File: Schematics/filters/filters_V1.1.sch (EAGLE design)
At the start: 110 parts, among them IC1 NE5532N, IC2 NE5532N, IC3 NE5532N, IC4 NE5532N, IC5 NE5532N, IC6 NE5532N, IC7 NE5532N, J1 3_PIN_AMPCONN, J2 4_PIN_AMPCONN, J3 3_PIN_AMPCONN

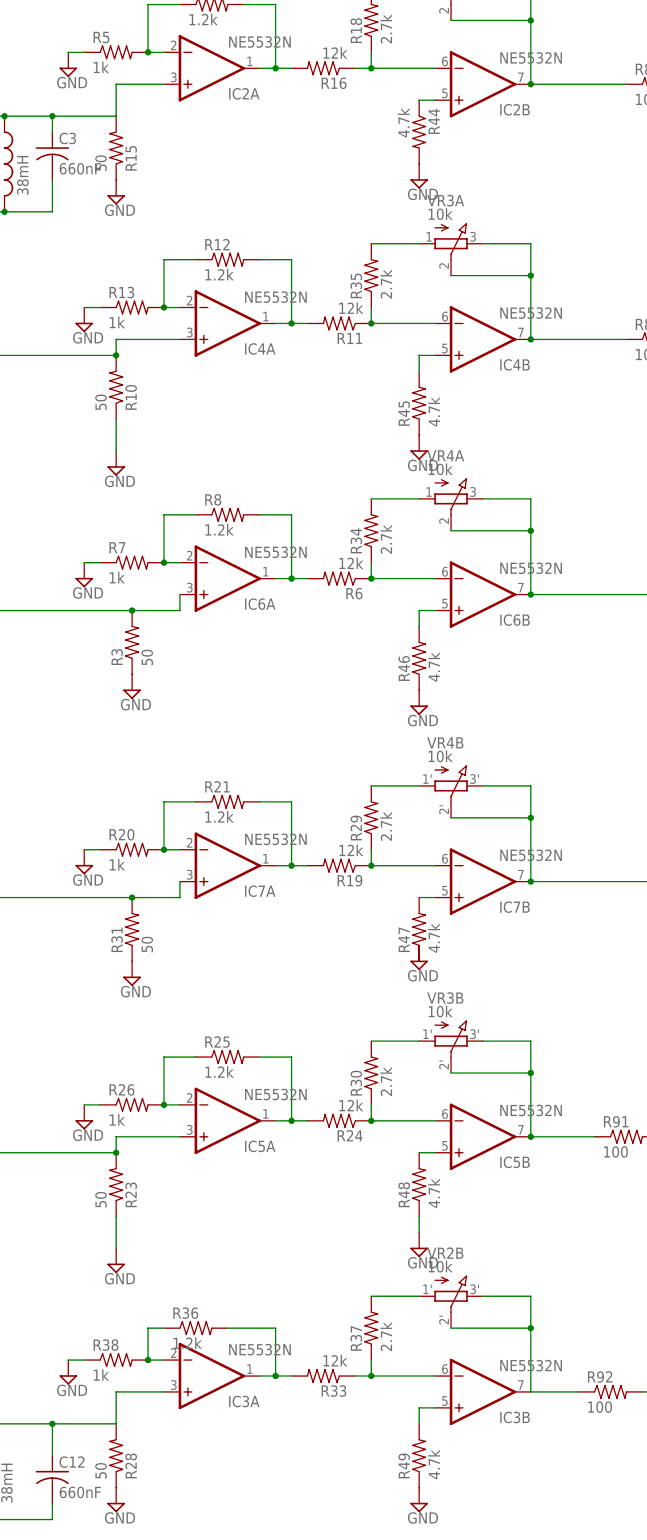
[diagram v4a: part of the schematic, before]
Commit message: Updated low pass filter amplifier with increased gain. Added filter response measurements
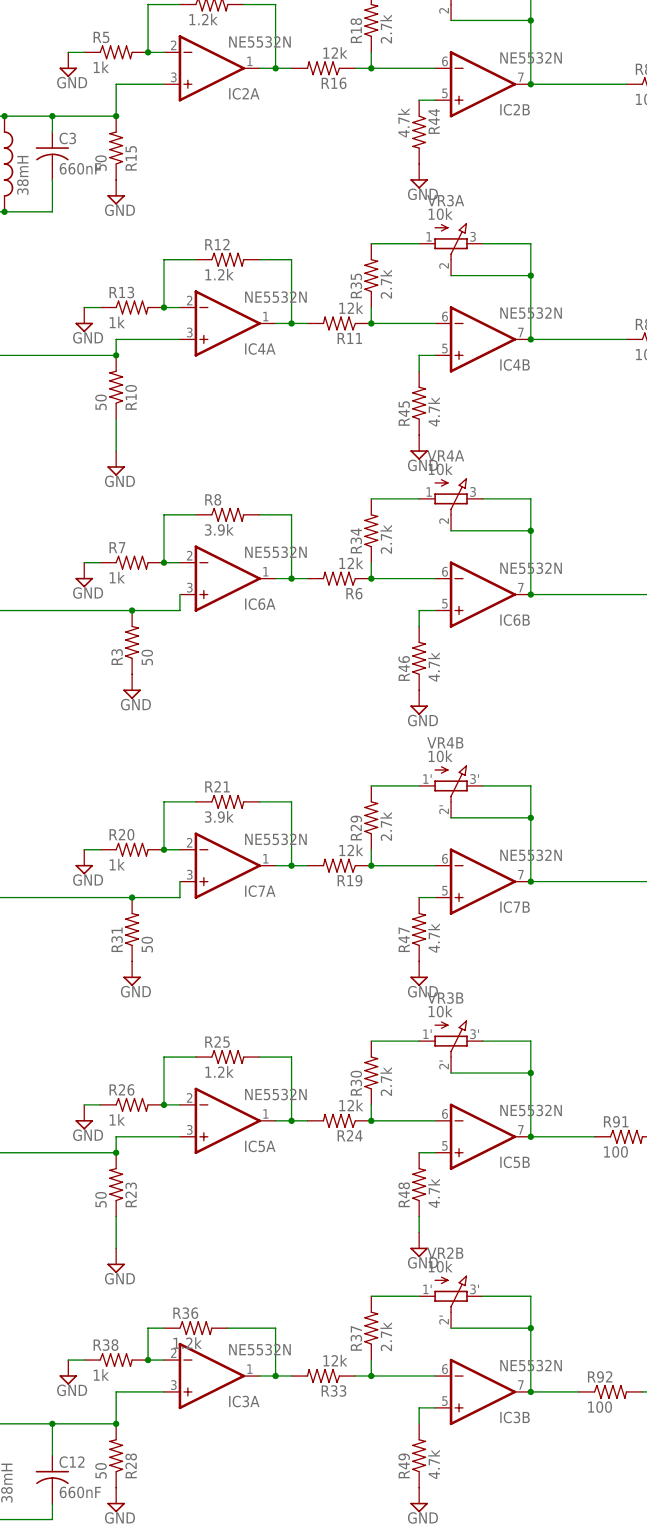
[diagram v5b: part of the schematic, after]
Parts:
- R21, R8: value 1.2k -> 3.9k
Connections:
- net GND: now also R47.1
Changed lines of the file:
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@@
 <part name="R6" library="rcl" deviceset="R-US_" device="0204/2V" value="12k"/>
 <part name="R7" library="rcl" deviceset="R-US_" device="0204/2V" value="1k"/>
-<part name="R8" library="rcl" deviceset="R-US_" device="0204/2V" value="1.2k"/>
+<part name="R8" library="rcl" deviceset="R-US_" device="0204/2V" value="3.9k"/>
 <part name="R9" library="rcl" deviceset="R-US_" device="0204/2V" value="50"/>
 <part name="R10" library="rcl" deviceset="R-US_" device="0204/2V" value="50"/>
@@
 <part name="R19" library="rcl" deviceset="R-US_" device="0204/2V" value="12k"/>
 <part name="R20" library="rcl" deviceset="R-US_" device="0204/2V" value="1k"/>
-<part name="R21" library="rcl" deviceset="R-US_" device="0204/2V" value="1.2k"/>
+<part name="R21" library="rcl" deviceset="R-US_" device="0204/2V" value="3.9k"/>
 <part name="R22" library="rcl" deviceset="R-US_" device="0204/2V" value="50"/>
 <part name="R23" library="rcl" deviceset="R-US_" device="0204/2V" value="50"/>
@@
 <part name="R37" library="rcl" deviceset="R-US_" device="0204/2V" value="2.7k"/>
 <part name="R38" library="rcl" deviceset="R-US_" device="0204/2V" value="1k"/>
-<part name="GND4" library="supply2" deviceset="GND" device=""/>
 <part name="GND5" library="supply2" deviceset="GND" device=""/>
 <part name="GND6" library="supply2" deviceset="GND" device=""/>
@@
 <part name="R45" library="rcl" deviceset="R-US_" device="0204/2V" value="4.7k"/>
 <part name="R46" library="rcl" deviceset="R-US_" device="0204/2V" value="4.7k"/>
-<part name="R47" library="rcl" deviceset="R-US_" device="0204/2V" value="4.7k"/>
 <part name="R48" library="rcl" deviceset="R-US_" device="0204/2V" value="4.7k"/>
 <part name="R49" library="rcl" deviceset="R-US_" device="0204/2V" value="4.7k"/>
@@
 <part name="J2" library="Amplifier_Parts" deviceset="4_PIN_AMPCONN" device=""/>
 <part name="GND27" library="supply2" deviceset="GND" device=""/>
+<part name="R47" library="rcl" deviceset="R-US_" device="0204/2V" value="4.7k"/>
+<part name="GND4" library="supply2" deviceset="GND" device=""/>
 </parts>
 <sheets>
@@
 <instance part="R37" gate="G$1" x="304.8" y="88.9" rot="R90"/>
 <instance part="R38" gate="G$1" x="264.16" y="83.82"/>
-<instance part="GND4" gate="GND" x="312.42" y="147.32"/>
 <instance part="GND5" gate="GND" x="312.42" y="101.6"/>
 <instance part="GND6" gate="GND" x="312.42" y="60.96"/>
@@
 <instance part="R45" gate="G$1" x="312.42" y="236.22" rot="R90"/>
 <instance part="R46" gate="G$1" x="312.42" y="195.58" rot="R90"/>
-<instance part="R47" gate="G$1" x="312.42" y="152.4" rot="R90"/>
 <instance part="R48" gate="G$1" x="312.42" y="111.76" rot="R90"/>
 <instance part="R49" gate="G$1" x="312.42" y="68.58" rot="R90"/>
@@
 <instance part="J2" gate="G$1" x="482.6" y="180.34" rot="MR0"/>
 <instance part="GND27" gate="GND" x="474.98" y="170.18"/>
+<instance part="R47" gate="G$1" x="312.42" y="152.4" rot="R90"/>
+<instance part="GND4" gate="GND" x="312.42" y="144.78"/>
 </instances>
 <busses>
@@
 <pinref part="J2" gate="G$1" pin="4"/>
 <wire x1="474.98" y1="175.26" x2="477.52" y2="175.26" width="0.1524" layer="91"/>
+</segment>
+<segment>
+<pinref part="R47" gate="G$1" pin="1"/>
+<pinref part="GND4" gate="GND" pin="GND"/>
 </segment>
 </net>
@@
 <pinref part="IC2" gate="A" pin="+IN"/>
 <wire x1="264.16" y1="287.02" x2="271.78" y2="287.02" width="0.1524" layer="91"/>
+<junction x="264.16" y="281.94"/>
 </segment>
 </net>
@@
 <junction x="330.2" y="88.9"/>
 <pinref part="R92" gate="G$1" pin="1"/>
+<junction x="330.2" y="78.74"/>
 </segment>
 </net>
@@
 <pinref part="IC3" gate="A" pin="+IN"/>
 <wire x1="271.78" y1="78.74" x2="264.16" y2="78.74" width="0.1524" layer="91"/>
+<junction x="264.16" y="73.66"/>
 </segment>
 </net>
@@
 <segment>
 <pinref part="IC7" gate="B" pin="+IN"/>
+<wire x1="314.96" y1="157.48" x2="312.42" y2="157.48" width="0.1524" layer="91"/>
 <pinref part="R47" gate="G$1" pin="2"/>
-<wire x1="314.96" y1="157.48" x2="312.42" y2="157.48" width="0.1524" layer="91"/>
 </segment>
 </net>
@@
 </sheet>
 </sheets>
+<errors>
+</errors>
 </schematic>
 </drawing>

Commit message: added names to input and output traces on filter board
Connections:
- net N$10 renamed RIGHT
- net N$108 renamed LEFT_IN
- net N$19 renamed BASS
- net N$26 renamed RIGHT_IN
- net N$38 renamed LEFT
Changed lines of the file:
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@@
 <?xml version="1.0" encoding="utf-8"?>
 <!DOCTYPE eagle SYSTEM "eagle.dtd">
-<eagle version="7.4.0">
+<eagle version="6.5.0">
 <drawing>
 <settings>
@@
 </segment>
 </net>
-<net name="N$26" class="0">
+<net name="RIGHT_IN" class="0">
 <segment>
 <wire x1="99.06" y1="198.12" x2="116.84" y2="198.12" width="0.1524" layer="91"/>
@@
 </segment>
 </net>
-<net name="N$108" class="0">
+<net name="LEFT_IN" class="0">
 <segment>
 <wire x1="99.06" y1="195.58" x2="116.84" y2="195.58" width="0.1524" layer="91"/>
@@
 </segment>
 </net>
-<net name="N$10" class="0">
+<net name="RIGHT" class="0">
 <segment>
 <pinref part="R89" gate="G$1" pin="2"/>
@@
 </segment>
 </net>
-<net name="N$38" class="0">
+<net name="LEFT" class="0">
 <segment>
 <pinref part="R91" gate="G$1" pin="2"/>
@@
 </segment>
 </net>
-<net name="N$19" class="0">
+<net name="BASS" class="0">
 <segment>
 <pinref part="R90" gate="G$1" pin="2"/>
